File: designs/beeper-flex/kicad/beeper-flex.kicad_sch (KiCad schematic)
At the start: 5 parts, among them U3 IM69D130V01XTSA1, U4 IM69D130V01XTSA1, U6 Edge-FH19C-6S-0.5SH(10)

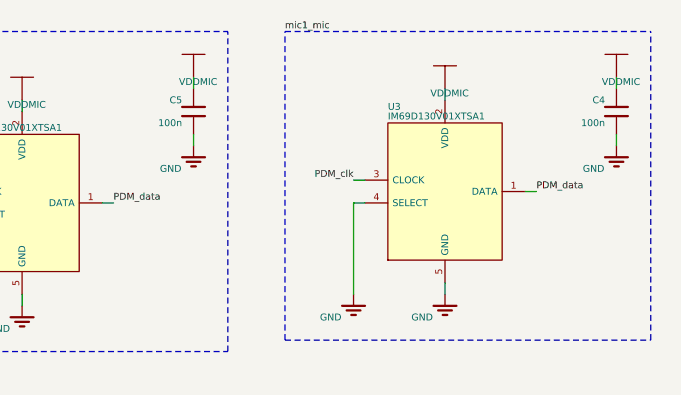
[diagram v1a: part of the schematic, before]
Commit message: added 3d model + fixed directory
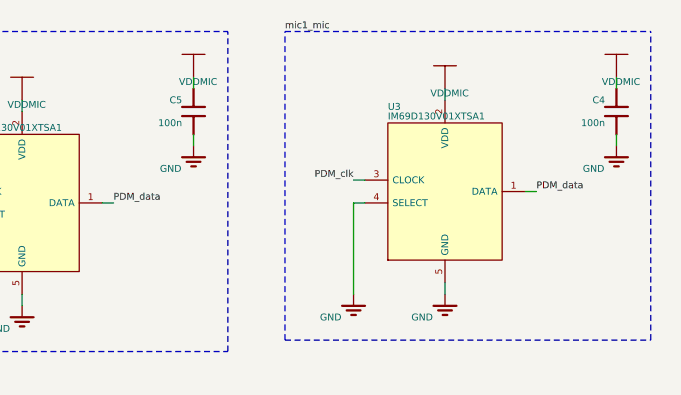
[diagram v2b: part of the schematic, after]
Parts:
- C4, C5: MPN GMC02X5R104K10NT -> CC0201MRX5R6BB104; Manufacturer Cal-Chip Electronics -> YAGEO

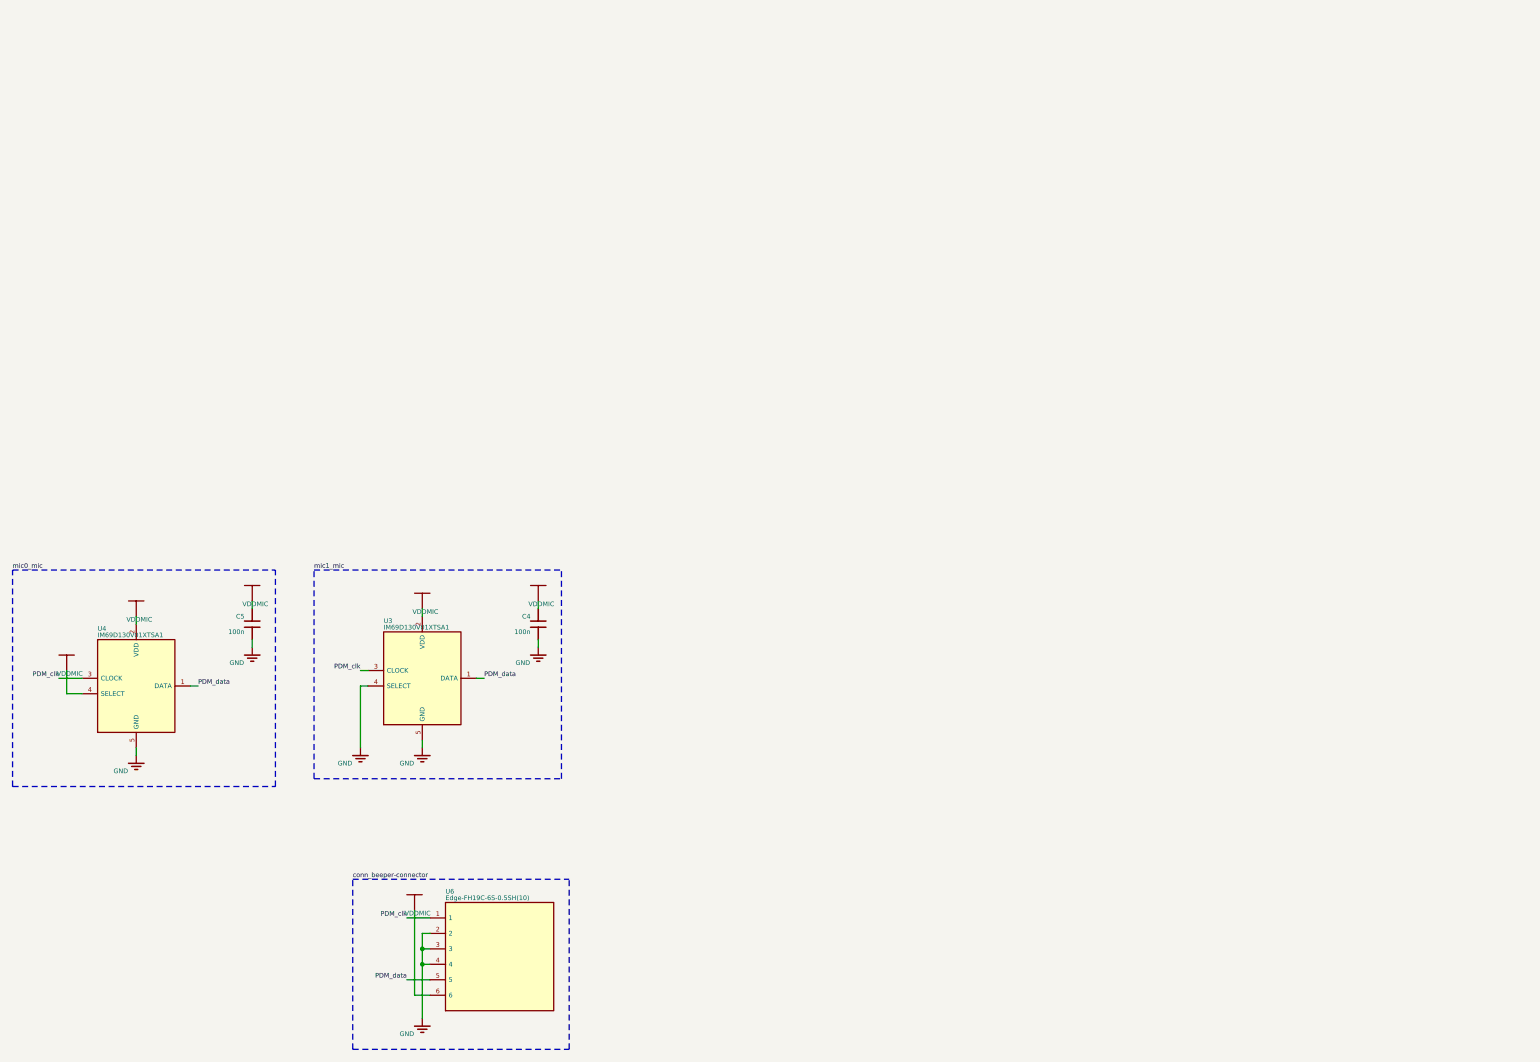
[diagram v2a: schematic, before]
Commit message: added flex data
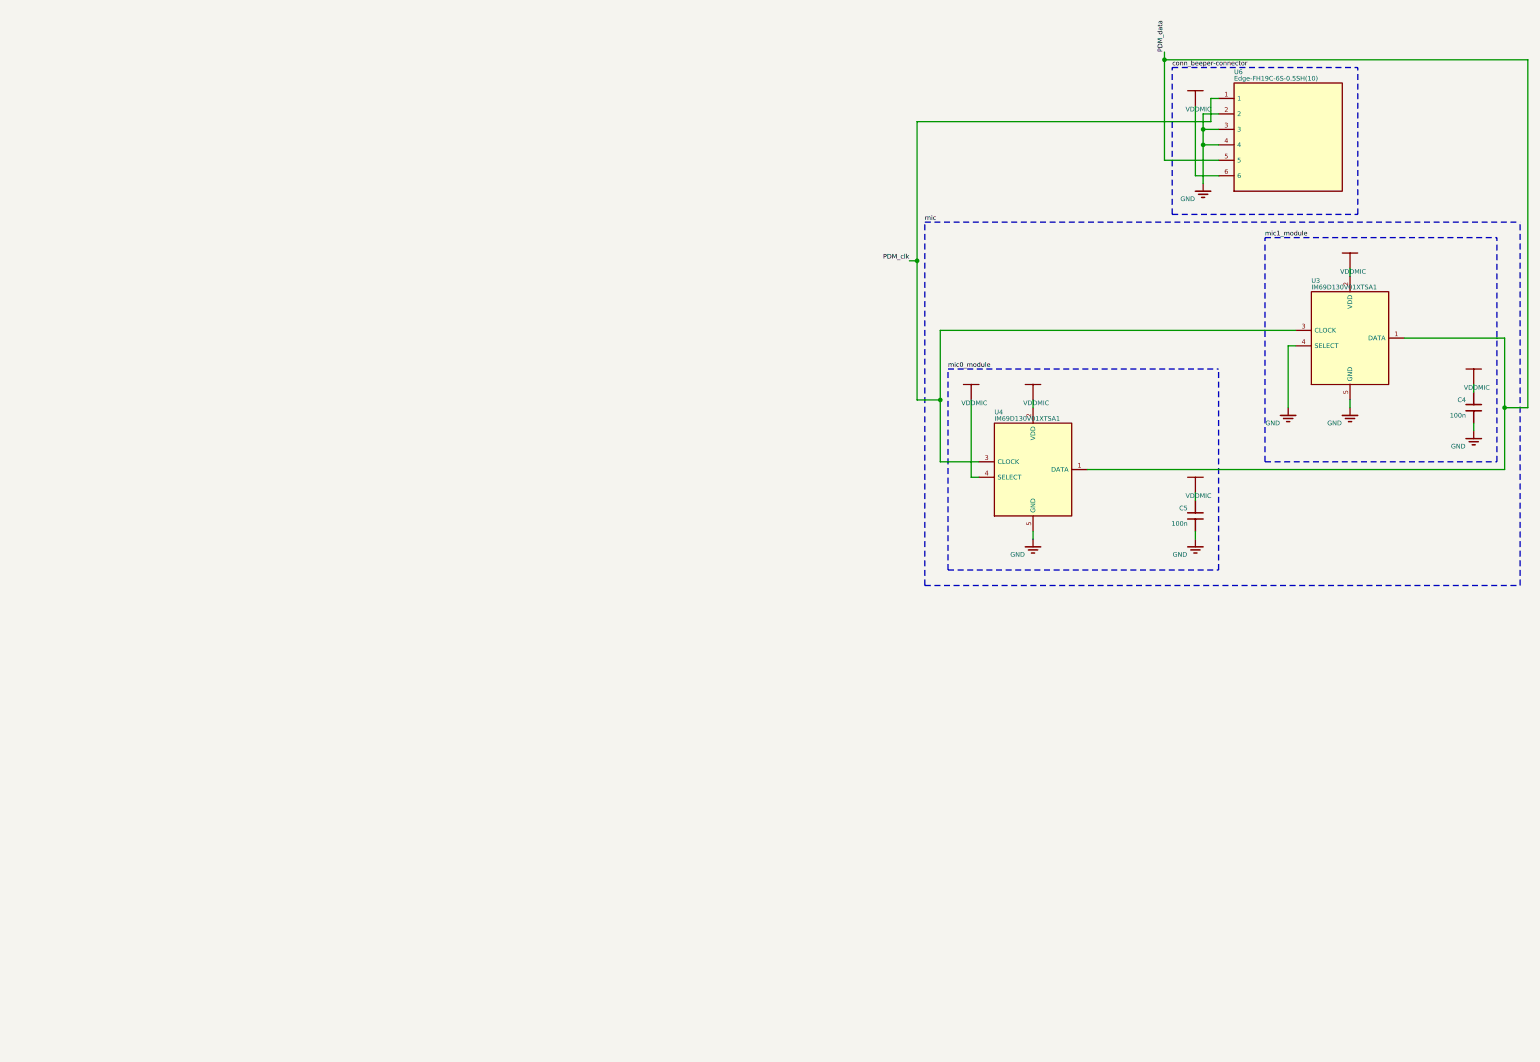
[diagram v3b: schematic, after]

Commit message: flex to cad with wrong rules
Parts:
- C4, C5: LCSC (none) -> C1853386
- U3, U4: LCSC (none) -> C9900035948
- U6: now not fitted; now left out of the parts list
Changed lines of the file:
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@@
   (wire (pts (xy 267.97 142.24) (xy 267.97 85.09)) (stroke (width 0.127) (type default) (color 0 0 0 0)))
   (wire (pts (xy 208.28 101.6) (xy 208.28 83.82)) (stroke (width 0.127) (type default) (color 0 0 0 0)))
+  (wire (pts (xy 168.91 140.97) (xy 171.45 140.97)) (stroke (width 0.127) (type default) (color 0 0 0 0)))
   (wire (pts (xy 171.45 151.13) (xy 172.72 151.13)) (stroke (width 0.127) (type default) (color 0 0 0 0)))
   (wire (pts (xy 171.45 129.54) (xy 224.79 129.54)) (stroke (width 0.127) (type default) (color 0 0 0 0)))
   (wire (pts (xy 171.45 151.13) (xy 171.45 129.54)) (stroke (width 0.127) (type default) (color 0 0 0 0)))
-  (wire (pts (xy 168.91 140.97) (xy 171.45 140.97)) (stroke (width 0.127) (type default) (color 0 0 0 0)))
   (wire (pts (xy 262.89 130.81) (xy 264.16 130.81)) (stroke (width 0.127) (type default) (color 0 0 0 0)))
   (wire (pts (xy 217.17 152.4) (xy 264.16 152.4)) (stroke (width 0.127) (type default) (color 0 0 0 0)))
@@
       (property "Manufacturer" "Infineon" (id 6) (at 238.76 130.81 0.0) (effects (font (size 0.762 0.762)) hide))
       (property "MPN" "IM69D130V01XTSA1" (id 7) (at 238.76 130.81 0.0) (effects (font (size 0.762 0.762)) hide))
+      (property "LCSC" "C9900035948" (id 8) (at 238.76 130.81 0.0) (effects (font (size 0.762 0.762)) hide))
     (pin "CLOCK")
     (pin "SELECT")
@@
       (property "MPN" "CC0201MRX5R6BB104" (id 7) (at 213.36 160.02 180.0) (effects (font (size 0.762 0.762)) hide))
       (property "Reference-prefix" "C" (id 8) (at 213.36 160.02 180.0) (effects (font (size 0.762 0.762)) hide))
+      (property "LCSC" "C1853386" (id 9) (at 213.36 160.02 180.0) (effects (font (size 0.762 0.762)) hide))
     (pin "1")
     (pin "2")
@@
   )
   (symbol (lib_id "edge_FH19C_6S_0_5SH_10_") (at 228.6 97.79 0.0)  (unit 1)
-    (in_bom yes) (on_board yes)
+    (in_bom no) (on_board yes) (dnp yes)
     (property "Reference" "U6" (id 0) (at 219.71 87.538 0.0) (effects (font (size 0.762 0.762)) (justify left bottom )))
     (property "Value" "Edge-FH19C-6S-0.5SH(10)" (id 1) (at 219.71 88.6 0.0) (effects (font (size 0.762 0.762)) (justify left bottom )))
@@
       (property "MPN" "CC0201MRX5R6BB104" (id 7) (at 259.08 142.24 180.0) (effects (font (size 0.762 0.762)) hide))
       (property "Reference-prefix" "C" (id 8) (at 259.08 142.24 180.0) (effects (font (size 0.762 0.762)) hide))
+      (property "LCSC" "C1853386" (id 9) (at 259.08 142.24 180.0) (effects (font (size 0.762 0.762)) hide))
     (pin "1")
     (pin "2")
@@
       (property "Manufacturer" "Infineon" (id 6) (at 186.69 152.4 0.0) (effects (font (size 0.762 0.762)) hide))
       (property "MPN" "IM69D130V01XTSA1" (id 7) (at 186.69 152.4 0.0) (effects (font (size 0.762 0.762)) hide))
+      (property "LCSC" "C9900035948" (id 8) (at 186.69 152.4 0.0) (effects (font (size 0.762 0.762)) hide))
     (pin "CLOCK")
     (pin "SELECT")
